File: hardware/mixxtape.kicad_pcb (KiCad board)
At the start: 2 copper layers, 100.3 x 63.5 mm, 0 parts

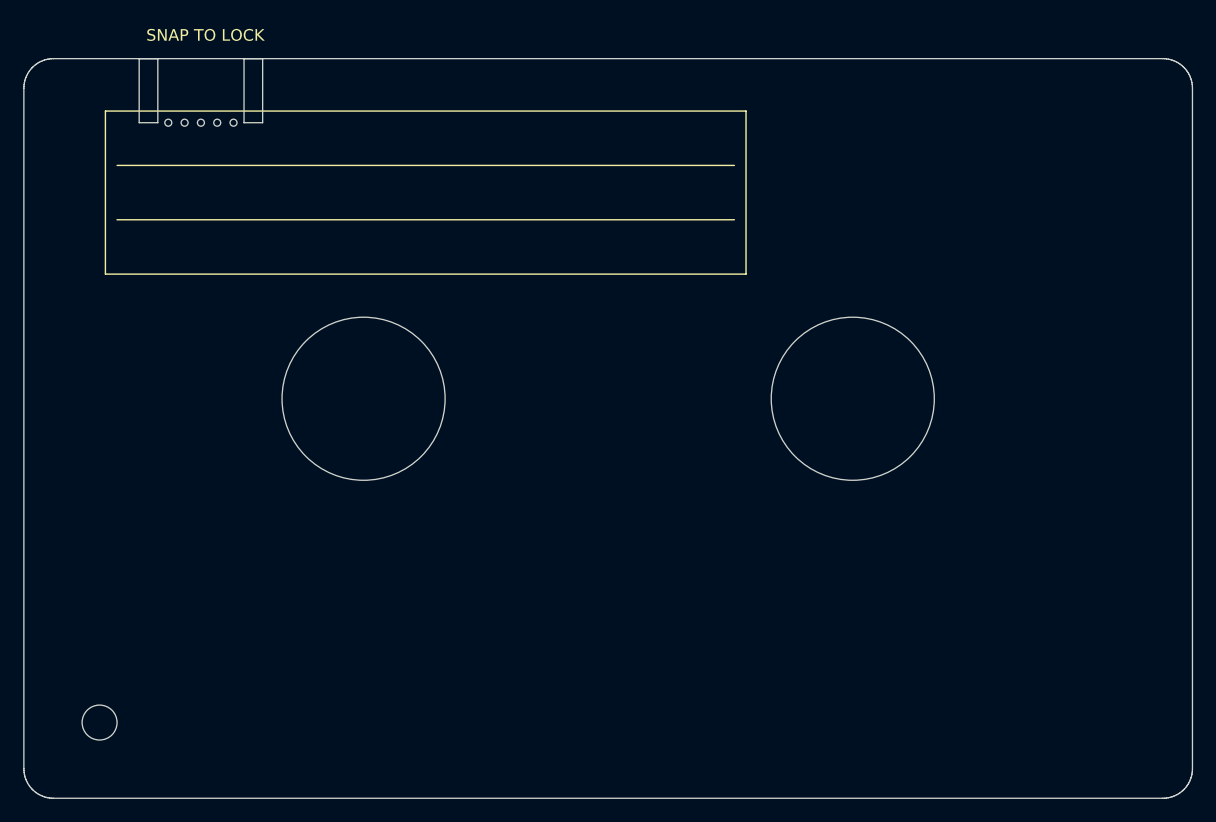
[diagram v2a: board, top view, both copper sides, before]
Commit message: hardware: pre-routing review — outline, pin types, TAB1, battery removal
Checked every footprint and every net before routing starts.

The board outline was self-intersecting and would have failed CAM. The
write-protect tab's two slots were drawn as closed rectangles lying on top
of the top edge instead of cut into it, so the edge ran straight through
both. Split the top edge into three spans and removed the slot mouths.

Every symbol pin now has a real electrical type. easyeda2kicad types every
pin "unspecified", which silently disables the checks that matter, so ERC
was reporting 191 warnings of one meaningless class and nothing else. 109
pins retyped from the datasheets, in the schematic and in the library so a
library update cannot undo it. That immediately found three genuine faults:
U4's two VOUT pins and J1's paired VBUS and GND pins each read as two power
outputs fighting over one rail. ERC is now 0.

TAB1 had no footprint, so TAB_SENSE would have read permanently low. Added
TAB_BREAKOFF_LINK, a two-pad net tie on the break-off tongue.

The battery section is removed. U5, J2 and R8 were always DNP and could
never have worked: a lithium cell at 3.0-4.2 V cannot feed an AMS1117 that
needs 1.1-1.3 V of headroom, and the LEDs sit on the 5 V USB rail besides.

Datasheet-driven part changes: C9 100 nF -> 1 uF on EN, which is what the
ESP32-WROOM-32E datasheet asks for, and a new R12 100 R in the microphone's
supply per figure 1 of the MSM261DHT006 datasheet, with C7 moved onto
MIC_VDD so the two actually form a filter.

Also: three mounting holes, four zero-annulus locating pegs made non-plated,
a DRC rule scoping J1's 0.10 mm internal pad spacing, and corrected datasheet
links (the LEDs pointed at Worldsemi while the fitted part is XINGLIGHT).

Verified: ERC 0, DRC clean apart from the 130 unrouted nets, every
footprint's pads reconcile with its symbol's pins, and every board pad
agrees with the schematic netlist.

Co-Authored-By: Claude Opus 5 <noreply@anthropic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
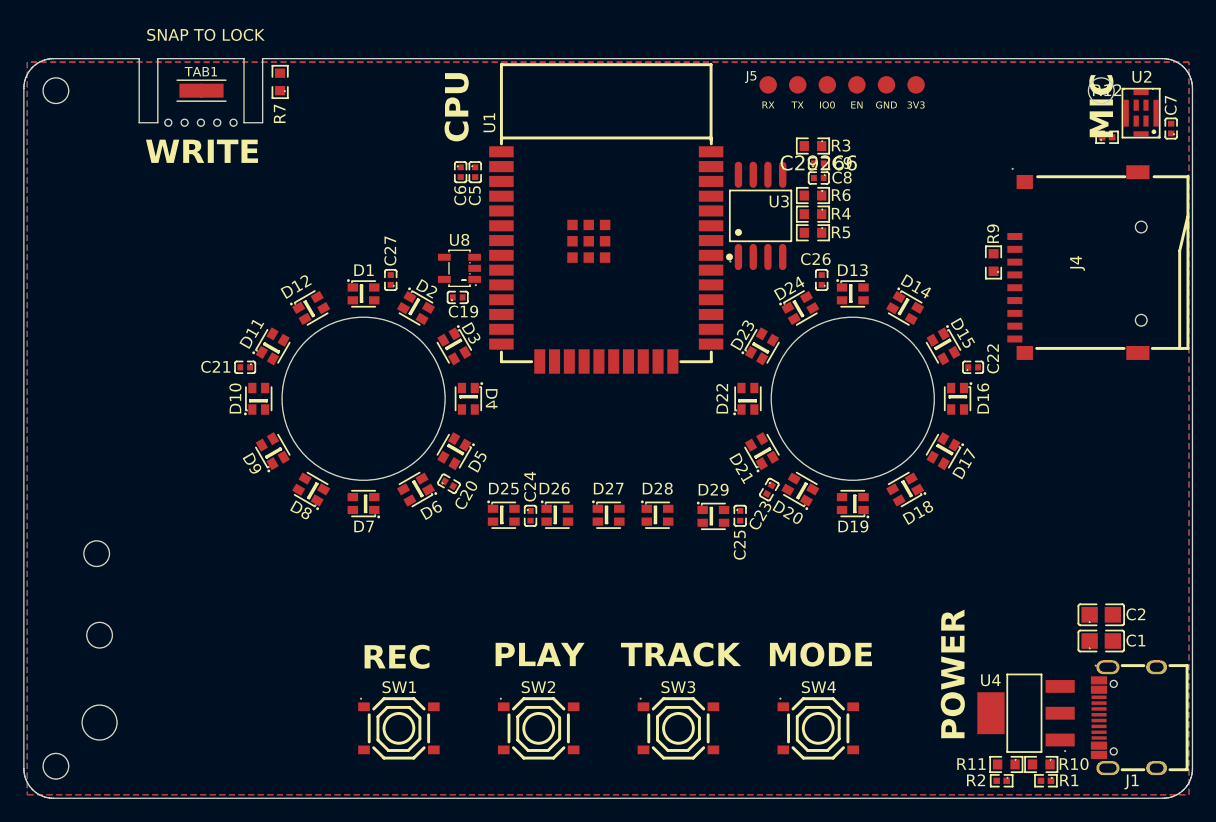
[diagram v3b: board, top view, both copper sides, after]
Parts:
- added C1: C0805, C0805, F.Cu at (122.5, 80.0)
- added C19: C0402, C0402, F.Cu at (67.2, 50.5)
- added C2: C0805, C0805, F.Cu at (122.5, 77.8)
- added C20: C0402, C0402, F.Cu at (66.5, 66.5)
- added C21: C0402, C0402, F.Cu at (49.0, 56.5)
- added C22: C0402, C0402, F.Cu at (111.5, 56.5)
- added C23: C0402, C0402, F.Cu at (94.0, 67.0)
- added C24: C0402, C0402, F.Cu at (73.5, 69.2)
- added C25: C0402, C0402, F.Cu at (91.5, 69.2)
- added C26: C0402, C0402, F.Cu at (98.5, 49.0)
- added C27: C0402, C0402, F.Cu at (61.5, 49.0)
- added C5: C0402, C0402, F.Cu at (68.8, 39.8)
- added C6: C0402, C0402, F.Cu at (67.5, 39.8)
- added C7: C0402, C0402, F.Cu at (128.5, 36.0)
- added C8: C0402, C0402, F.Cu at (98.2, 40.2)
- added C9: 1uF, C0402, F.Cu at (98.2, 39.0)
- added D1: LED-SMD_4P-L2.0-W2.0-TL_WS2812B-2020, LED-SMD_4P-L2.0-W2.0-TL_WS2812B-2020, F.Cu at (59.2, 50.2)
- added D10: LED-SMD_4P-L2.0-W2.0-TL_WS2812B-2020, LED-SMD_4P-L2.0-W2.0-TL_WS2812B-2020, F.Cu at (50.2, 59.2)
- added D11: LED-SMD_4P-L2.0-W2.0-TL_WS2812B-2020, LED-SMD_4P-L2.0-W2.0-TL_WS2812B-2020, F.Cu at (51.4, 54.7)
- added D12: LED-SMD_4P-L2.0-W2.0-TL_WS2812B-2020, LED-SMD_4P-L2.0-W2.0-TL_WS2812B-2020, F.Cu at (54.7, 51.4)
- added D13: LED-SMD_4P-L2.0-W2.0-TL_WS2812B-2020, LED-SMD_4P-L2.0-W2.0-TL_WS2812B-2020, F.Cu at (101.2, 50.2)
- added D14: LED-SMD_4P-L2.0-W2.0-TL_WS2812B-2020, LED-SMD_4P-L2.0-W2.0-TL_WS2812B-2020, F.Cu at (105.7, 51.4)
- added D15: LED-SMD_4P-L2.0-W2.0-TL_WS2812B-2020, LED-SMD_4P-L2.0-W2.0-TL_WS2812B-2020, F.Cu at (109.0, 54.7)
- added D16: LED-SMD_4P-L2.0-W2.0-TL_WS2812B-2020, LED-SMD_4P-L2.0-W2.0-TL_WS2812B-2020, F.Cu at (110.2, 59.2)
- added D17: LED-SMD_4P-L2.0-W2.0-TL_WS2812B-2020, LED-SMD_4P-L2.0-W2.0-TL_WS2812B-2020, F.Cu at (109.0, 63.7)
- added D18: LED-SMD_4P-L2.0-W2.0-TL_WS2812B-2020, LED-SMD_4P-L2.0-W2.0-TL_WS2812B-2020, F.Cu at (105.7, 67.0)
- added D19: LED-SMD_4P-L2.0-W2.0-TL_WS2812B-2020, LED-SMD_4P-L2.0-W2.0-TL_WS2812B-2020, F.Cu at (101.2, 68.2)
- added D2: LED-SMD_4P-L2.0-W2.0-TL_WS2812B-2020, LED-SMD_4P-L2.0-W2.0-TL_WS2812B-2020, F.Cu at (63.7, 51.4)
- added D20: LED-SMD_4P-L2.0-W2.0-TL_WS2812B-2020, LED-SMD_4P-L2.0-W2.0-TL_WS2812B-2020, F.Cu at (96.7, 67.0)
- added D21: LED-SMD_4P-L2.0-W2.0-TL_WS2812B-2020, LED-SMD_4P-L2.0-W2.0-TL_WS2812B-2020, F.Cu at (93.4, 63.7)
- added D22: LED-SMD_4P-L2.0-W2.0-TL_WS2812B-2020, LED-SMD_4P-L2.0-W2.0-TL_WS2812B-2020, F.Cu at (92.2, 59.2)
- added D23: LED-SMD_4P-L2.0-W2.0-TL_WS2812B-2020, LED-SMD_4P-L2.0-W2.0-TL_WS2812B-2020, F.Cu at (93.4, 54.7)
- added D24: LED-SMD_4P-L2.0-W2.0-TL_WS2812B-2020, LED-SMD_4P-L2.0-W2.0-TL_WS2812B-2020, F.Cu at (96.7, 51.4)
- added D25: LED-SMD_4P-L2.0-W2.0-TL_WS2812B-2020, LED-SMD_4P-L2.0-W2.0-TL_WS2812B-2020, F.Cu at (71.2, 69.2)
- added D26: LED-SMD_4P-L2.0-W2.0-TL_WS2812B-2020, LED-SMD_4P-L2.0-W2.0-TL_WS2812B-2020, F.Cu at (75.8, 69.2)
- added D27: LED-SMD_4P-L2.0-W2.0-TL_WS2812B-2020, LED-SMD_4P-L2.0-W2.0-TL_WS2812B-2020, F.Cu at (80.2, 69.2)
- added D28: LED-SMD_4P-L2.0-W2.0-TL_WS2812B-2020, LED-SMD_4P-L2.0-W2.0-TL_WS2812B-2020, F.Cu at (84.4, 69.2)
- added D29: LED-SMD_4P-L2.0-W2.0-TL_WS2812B-2020, LED-SMD_4P-L2.0-W2.0-TL_WS2812B-2020, F.Cu at (89.2, 69.3)
- added D3: LED-SMD_4P-L2.0-W2.0-TL_WS2812B-2020, LED-SMD_4P-L2.0-W2.0-TL_WS2812B-2020, F.Cu at (67.0, 54.7)
- added D4: LED-SMD_4P-L2.0-W2.0-TL_WS2812B-2020, LED-SMD_4P-L2.0-W2.0-TL_WS2812B-2020, F.Cu at (68.2, 59.2)
- added D5: LED-SMD_4P-L2.0-W2.0-TL_WS2812B-2020, LED-SMD_4P-L2.0-W2.0-TL_WS2812B-2020, F.Cu at (67.0, 63.7)
- added D6: LED-SMD_4P-L2.0-W2.0-TL_WS2812B-2020, LED-SMD_4P-L2.0-W2.0-TL_WS2812B-2020, F.Cu at (63.7, 67.0)
- added D7: LED-SMD_4P-L2.0-W2.0-TL_WS2812B-2020, LED-SMD_4P-L2.0-W2.0-TL_WS2812B-2020, F.Cu at (59.2, 68.2)
- added D8: LED-SMD_4P-L2.0-W2.0-TL_WS2812B-2020, LED-SMD_4P-L2.0-W2.0-TL_WS2812B-2020, F.Cu at (54.7, 67.0)
- added D9: LED-SMD_4P-L2.0-W2.0-TL_WS2812B-2020, LED-SMD_4P-L2.0-W2.0-TL_WS2812B-2020, F.Cu at (51.4, 63.7)
- added J1: USB-C_SMD-TYPE-C-31-M-12_1, USB-C_SMD-TYPE-C-31-M-12_1, F.Cu at (124.8, 86.6)
- added J4: TF-SMD_TF-01A, TF-SMD_TF-01A, F.Cu at (120.4, 47.5)
- added J5: PROG_JIG, PROG_JIG_6PAD, F.Cu at (100.2, 32.2)
- added R1: R0402, R0402, F.Cu at (117.8, 92.0)
- added R10: R0603, R0603, F.Cu at (117.3, 90.6)
- added R11: R0603, R0603, F.Cu at (114.3, 90.6)
- added R12: 100R, R0402, F.Cu at (123.0, 36.8)
- added R2: R0402, R0402, F.Cu at (114.0, 92.0)
- added R3: R0603, R0603, F.Cu at (97.8, 37.5)
- added R4: R0603, R0603, F.Cu at (97.8, 43.4)
- added R5: R0603, R0603, F.Cu at (97.8, 45.0)
- added R6: R0603, R0603, F.Cu at (97.8, 41.8)
- added R7: R0603, R0603, F.Cu at (52.0, 32.0)
- added R9: R0603, R0603, F.Cu at (113.2, 47.5)
- added SW1: SW-SMD_4P-L5.1-W5.1-P3.70-LS6.5-TL_H1.5, SW-SMD_4P-L5.1-W5.1-P3.70-LS6.5-TL_H1.5, F.Cu at (62.2, 87.5)
- added SW2: SW-SMD_4P-L5.1-W5.1-P3.70-LS6.5-TL_H1.5, SW-SMD_4P-L5.1-W5.1-P3.70-LS6.5-TL_H1.5, F.Cu at (74.2, 87.5)
- added SW3: SW-SMD_4P-L5.1-W5.1-P3.70-LS6.5-TL_H1.5, SW-SMD_4P-L5.1-W5.1-P3.70-LS6.5-TL_H1.5, F.Cu at (86.2, 87.5)
- added SW4: SW-SMD_4P-L5.1-W5.1-P3.70-LS6.5-TL_H1.5, SW-SMD_4P-L5.1-W5.1-P3.70-LS6.5-TL_H1.5, F.Cu at (98.2, 87.5)
- added TAB1: WRITE-PROTECT, TAB_BREAKOFF_LINK, F.Cu at (45.2, 32.8)
- added U1: WIFI-SMD_ESP32-WROOM-32E, WIFI-SMD_ESP32-WROOM-32E, F.Cu at (80.0, 47.0)
- added U2: LGA-8_L4.0-W3.0-R_WMM7040DT0, LGA-8_L4.0-W3.0-R_WMM7040DT0, F.Cu at (125.9, 34.7)
- added U3: SOIC-8_L5.3-W5.3-P1.27-LS8.0-BL, SOIC-8_L5.3-W5.3-P1.27-LS8.0-BL, F.Cu at (93.2, 43.5)
- added U4: SOT-223-3_L6.5-W3.4-P2.30-LS7.0-BR, SOT-223-3_L6.5-W3.4-P2.30-LS7.0-BR, F.Cu at (116.0, 86.2)
- added U8: SOT-23-5_L3.0-W1.7-P0.95-LS2.8-BR, SOT-23-5_L3.0-W1.7-P0.95-LS2.8-BR, F.Cu at (67.4, 48.0)
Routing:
- added copper zone on B.Cu, net GND
- added copper zone on F.Cu, net GND
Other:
- outline, holes or cut-outs redrawn
- board text added: "CPU"
- board text added: "MIC"
- board text added: "MODE"
- board text added: "PLAY"
- board text added: "POWER"
- board text added: "REC"
- board text added: "TRACK"
- board text added: "WRITE"
